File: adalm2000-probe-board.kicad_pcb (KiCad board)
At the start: 2 copper layers, 60 x 60 mm, 15 parts, among them J1 ADALM200 INPUT, J2 MODULE OUTPUT, J3 CH1, J4 CH2, J5 V+/W1, J6 V-/W2, J7 V+/V- OUT, SW1 SW_CH1_CPL, SW2 SW_CH1_GND_REF, SW3 SW_CH2_CPL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

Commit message: Initial PCB design
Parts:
- added REF**: MountingHole_2.5mm_Pad_TopBottom, MountingHole:MountingHole_2.5mm_Pad_TopBottom, F.Cu at (121.0, 69.3)
- added REF**: MountingHole_2.5mm_Pad_TopBottom, MountingHole:MountingHole_2.5mm_Pad_TopBottom, F.Cu at (121.0, 123.1)
- added REF**: MountingHole_2.5mm_Pad_TopBottom, MountingHole:MountingHole_2.5mm_Pad_TopBottom, F.Cu at (174.6, 69.5)
- added REF**: MountingHole_2.5mm_Pad_TopBottom, MountingHole:MountingHole_2.5mm_Pad_TopBottom, F.Cu at (174.6, 122.9)
- J1: footprint Connector_IDC:IDC-Header_2x15_P2.54mm_Horizontal -> Jonnes Library:PinSocket_2x15_P2.54mm_Horizontal
- moved J1 20.0 mm to (147.7, 63.1), turned to 0 degrees

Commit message: Adding images and configuring board layers
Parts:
- added G***: LOGO, LOGO, F.Cu at (147.8, 94.1)
- added G***: LOGO, LOGO, B.Cu at (153.2, 114.4)
- added G***: LOGO, LOGO, B.Cu at (148.0, 93.9)
- moved J7 3.81 mm to (145.2, 108.6)
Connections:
- J3 pad 2: Net-(J3-Pad2) -> 1-
- J4 pad 2: Net-(J4-Pad2) -> 2-
- SW2 pad 2: Net-(J3-Pad2) -> 1-
- SW4 pad 2: Net-(J4-Pad2) -> 2-
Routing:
- added copper zone on In1.Cu, net GND1
- added copper zone on In2.Cu, net GND4
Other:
- board size 60 x 60 mm -> 59.9 x 60.2 mm
- copper layers 2 -> 4
- board text added: "ADALM2000 Probe Board Eng. Jonnes Nascimento"
- board text added: "Made in Brazil"
- board text added: "v1.0 - Dez. 2022"
- board text removed: "ADALM2000 Probe Board v1.0 Eng. Jonnes Nascimento Nov. 2022"
- board text removed: "Pesquisar qual o modelo de conector usado pelo ADALM200 para J1 e J2"

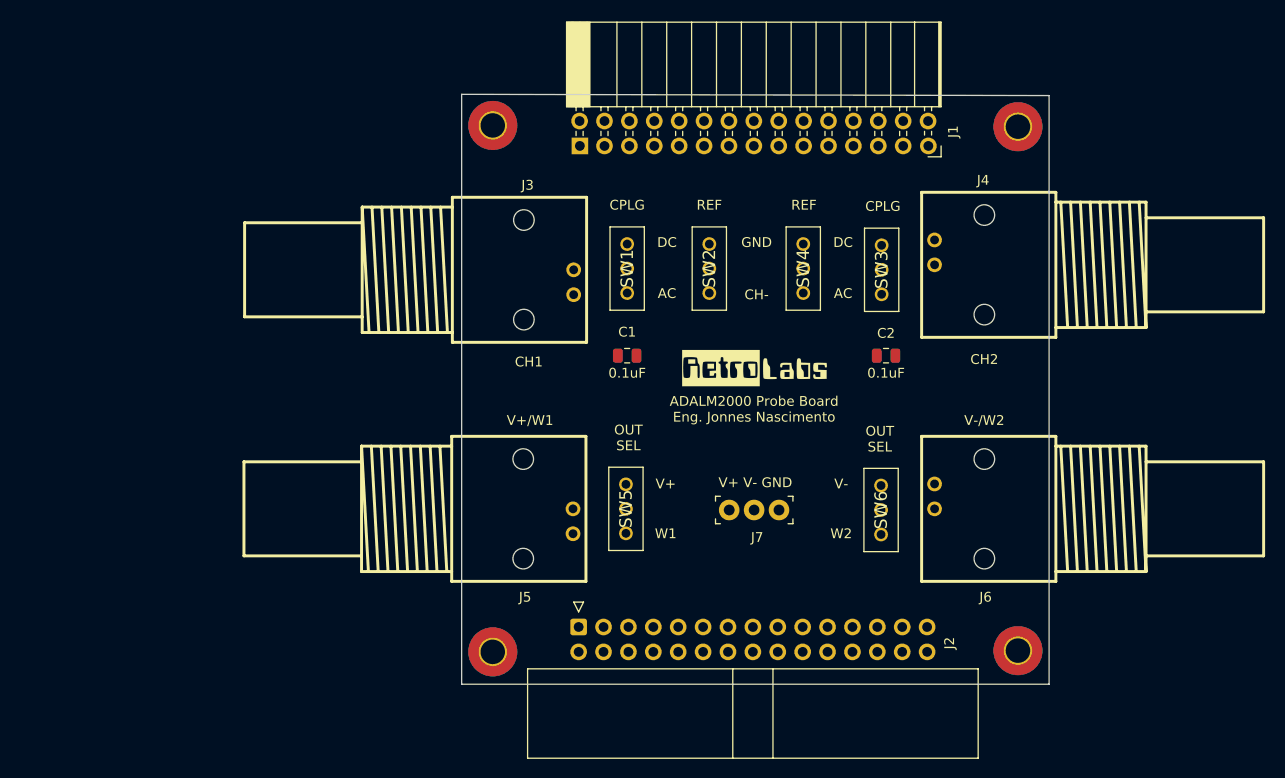
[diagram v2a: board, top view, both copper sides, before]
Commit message: Board initial routing
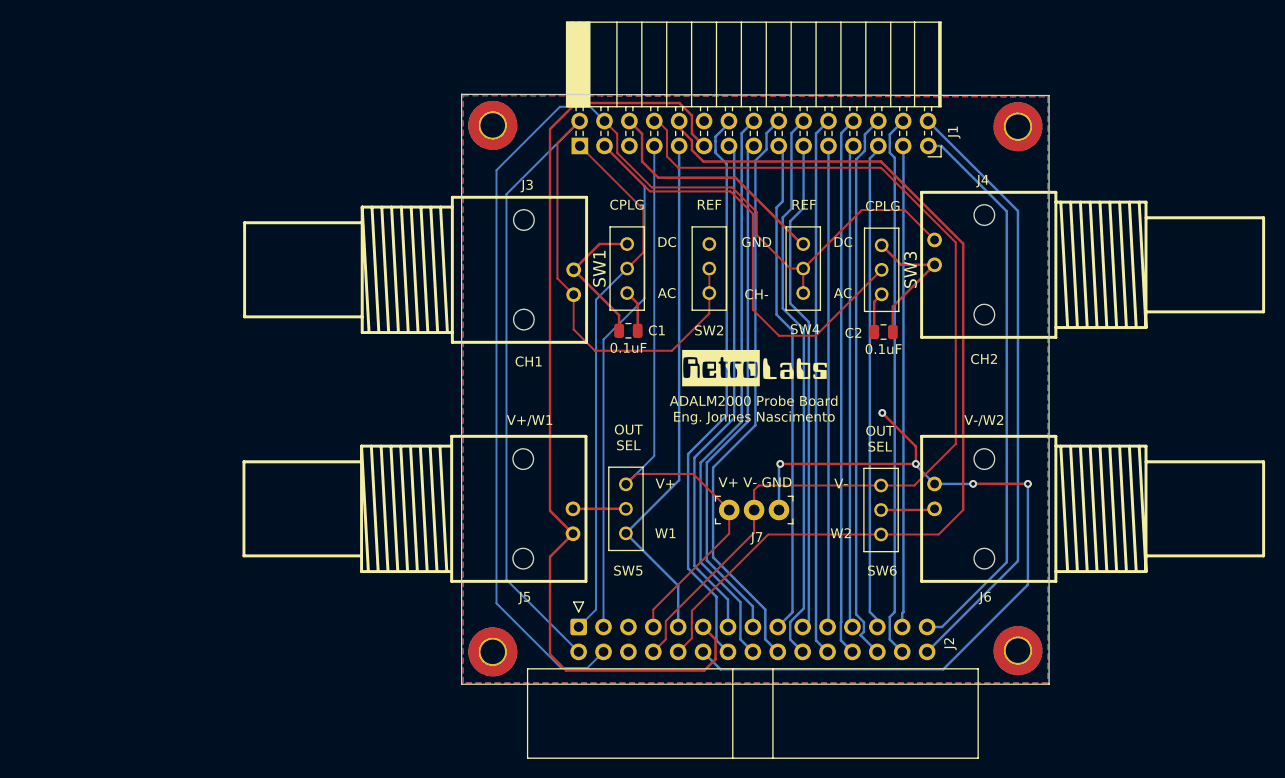
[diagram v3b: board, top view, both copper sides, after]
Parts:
- moved C1 2.54 mm to (134.9, 90.3)
- moved C2 2.43 mm to (160.9, 90.4)
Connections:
- J1 pad 10: W2 -> 2
- J1 pad 11: GND2 -> 3
- J1 pad 12: GND4 -> 4
- J1 pad 13: TI -> 5
- J1 pad 14: TO -> 6
- J1 pad 15: 0 -> 7
- J1 pad 16: 8 -> 1-
- J1 pad 17: 1 -> 2-
- J1 pad 18: 9 -> GND3
- J1 pad 19: 2 -> V-
- J1 pad 2: 1- -> 2+
- J1 pad 20: 10 -> W2
- J1 pad 21: 3 -> GND4
- J1 pad 22: 11 -> TO
- J1 pad 23: 4 -> 8
- J1 pad 24: 12 -> 9
- J1 pad 25: 5 -> 10
- J1 pad 26: 13 -> 11
- J1 pad 27: 6 -> 12
- J1 pad 28: 14 -> 13
- J1 pad 29: 7 -> 14
- J1 pad 3: 2+ -> GND1
- J1 pad 4: 2- -> V+
- J1 pad 5: GND1 -> W1
- J1 pad 6: GND3 -> GND2
- J1 pad 7: V+ -> TI
- J1 pad 8: V- -> 0
- J1 pad 9: W1 -> 1
- J2 pad 10: W2 -> 2
- J2 pad 11: GND2 -> 3
- J2 pad 12: GND4 -> 4
- J2 pad 13: TI -> 5
- J2 pad 14: TO -> 6
- J2 pad 15: 0 -> 7
- J2 pad 16: 8 -> 1-
- J2 pad 17: 1 -> 2-
- J2 pad 18: 9 -> GND3
- J2 pad 19: 2 -> V-
- J2 pad 2: 1- -> 2+
- J2 pad 20: 10 -> W2
- J2 pad 21: 3 -> GND4
- J2 pad 22: 11 -> TO
- J2 pad 23: 4 -> 8
- J2 pad 24: 12 -> 9
- J2 pad 25: 5 -> 10
- J2 pad 26: 13 -> 11
- J2 pad 27: 6 -> 12
- J2 pad 28: 14 -> 13
- J2 pad 29: 7 -> 14
- J2 pad 3: 2+ -> GND1
- J2 pad 4: 2- -> V+
- J2 pad 5: GND1 -> W1
- J2 pad 6: GND3 -> GND2
- J2 pad 7: V+ -> TI
- J2 pad 8: V- -> 0
- J2 pad 9: W1 -> 1
- REF** pad 1: (no net) -> GND2 (x2)
- REF** pad 1: (no net) -> GND4 (x2)
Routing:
- net 2-: track 0.00 -> 121.5 mm
- net 1-: track 0.00 -> 104.1 mm
- net V-: track 0.00 -> 101.3 mm
- net W2: track 0.00 -> 99.0 mm
- net 2+: track 0.00 -> 97.3 mm
- net GND2: track 0.00 -> 97.1 mm
- net GND4: track 0.00 -> 85.4 mm, vias 0 -> 5
- net V+: track 0.00 -> 63.4 mm
- net 15: track 0.00 -> 61.8 mm
- net 9: track 0.00 -> 59.7 mm
- net 8: track 0.00 -> 58.6 mm
- net TO: track 0.00 -> 58.5 mm
- net 7: track 0.00 -> 57.4 mm
- net 10: track 0.00 -> 57.1 mm
- net 13: track 0.00 -> 56.3 mm
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- added copper zone on F.Cu, net GND2
- added copper zone on In2.Cu, net GND3
- added copper zone on B.Cu, net GND4
- removed copper zone on In2.Cu, net GND4

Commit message: Board initial routing
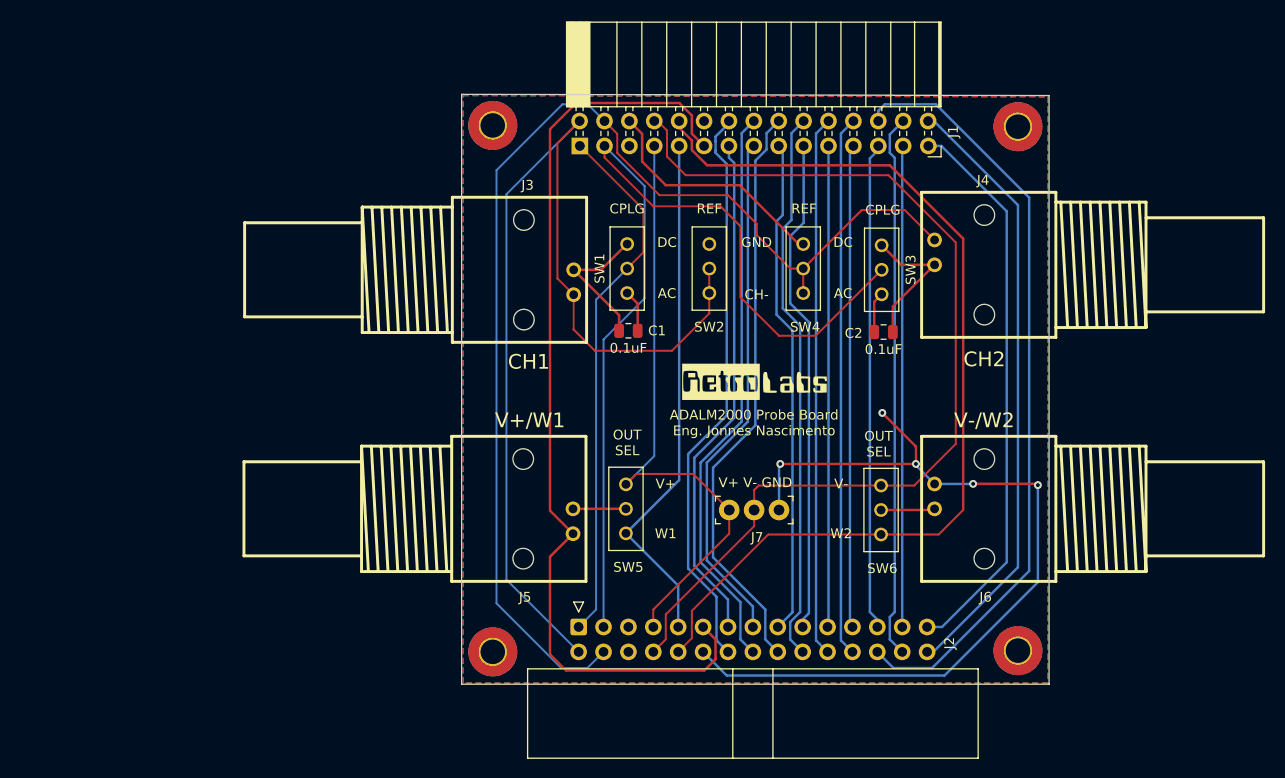
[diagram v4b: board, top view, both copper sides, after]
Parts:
- moved G*** 1.40 mm to (147.8, 95.5)
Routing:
- net 13: track 56.3 -> 79.0 mm
- net GND4: track 85.4 -> 87.7 mm
- net 2+: track 97.3 -> 96.5 mm
- net 15: track 61.8 -> 62.5 mm
